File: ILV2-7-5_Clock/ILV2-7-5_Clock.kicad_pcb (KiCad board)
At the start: 2 copper layers, 61 parts, among them J1 CONN_01X05, J2 USB_OTG, Q1 BSS84, Q2 BSS138, Q3 BSS84, Q4 BSS138, SW1 TACT_SWITCH, SW2 TACT_SWITCH, SW3 CJS1200, SW4 TACT_SWITCH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

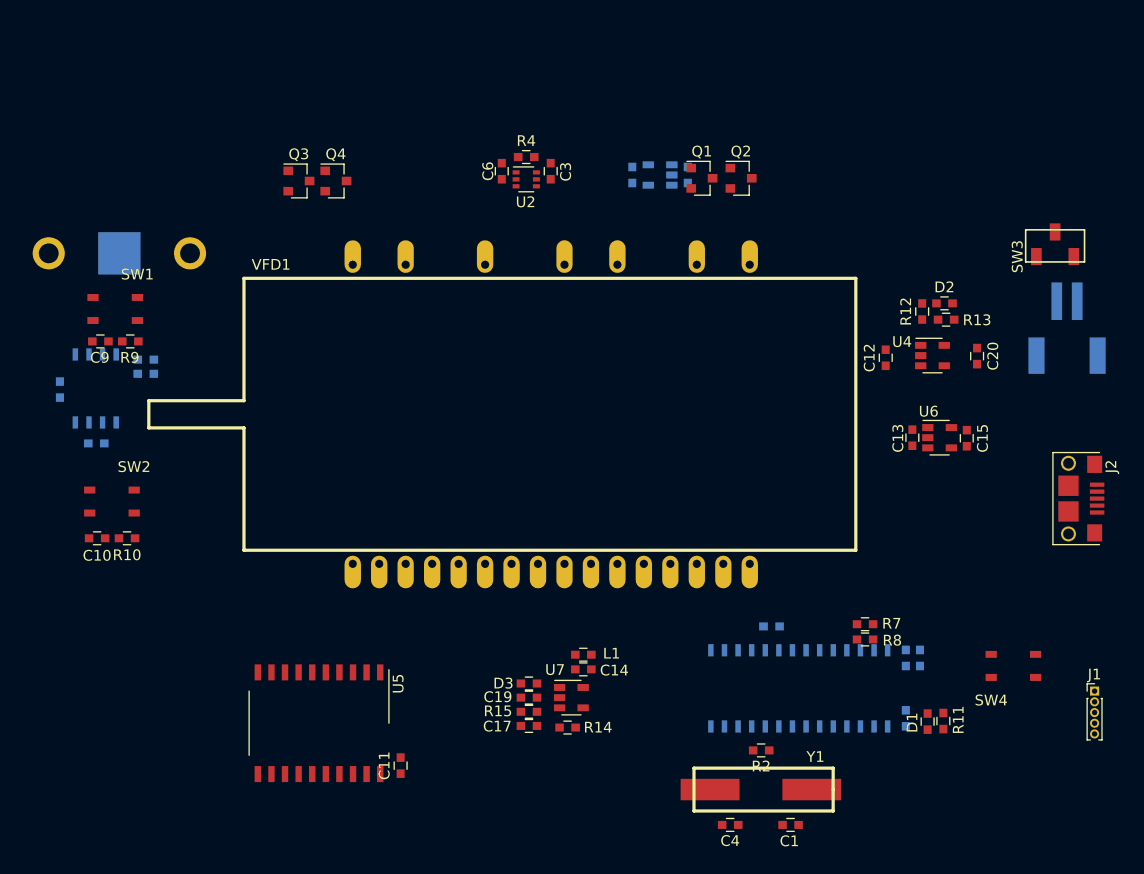
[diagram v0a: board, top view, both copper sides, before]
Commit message: More progress on the PCB and casing down schem issues
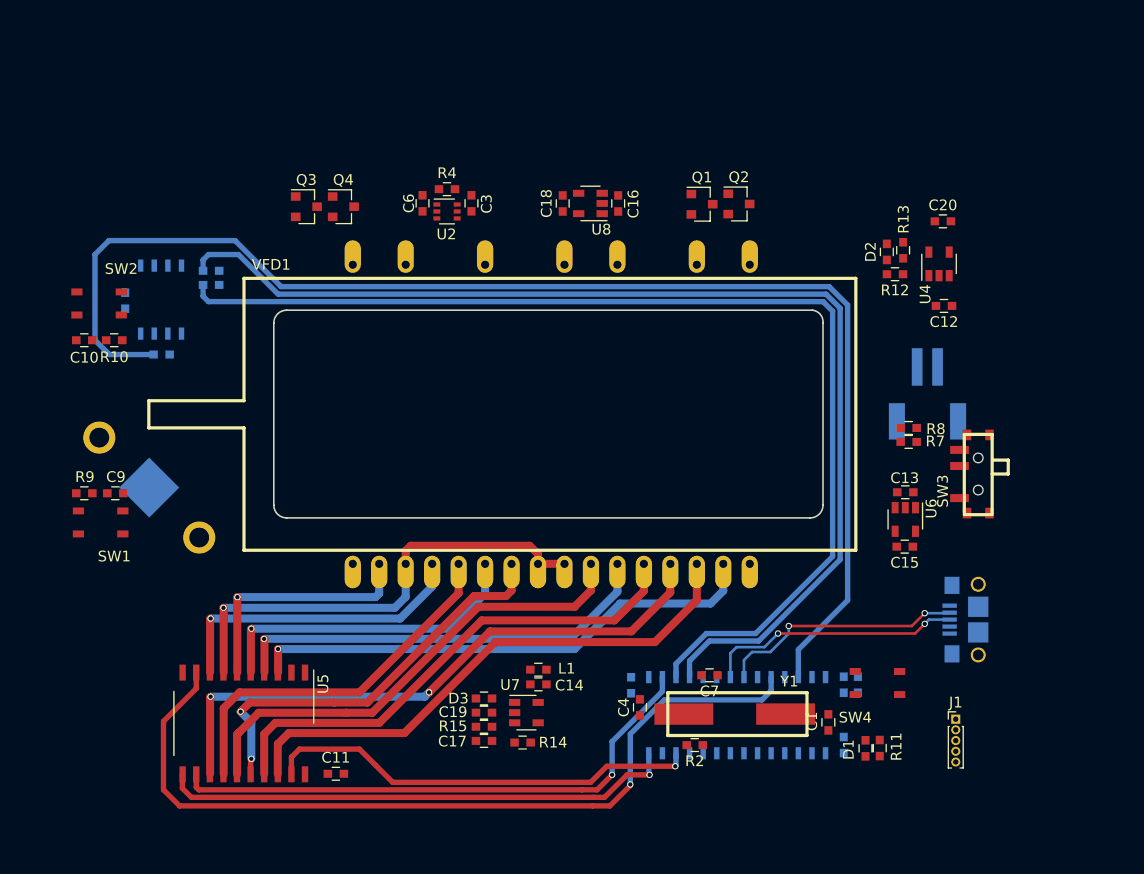
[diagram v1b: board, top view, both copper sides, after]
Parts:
- added C21: 1uF, Capacitors_SMD:C_0603, B.Cu at (151.4, 87.1)
- C16, C18, C7, U8: moved to F.Cu
- J2: moved to B.Cu
- SW3: value CJS1200 -> PCM12SMTR; footprint OpenBCI:CJS-1200TA -> Solutions:PCM12SMTR
- moved SW3 21.0 mm to (183.8, 67.4)
- moved SW1 20.7 mm to (102.7, 72.3), turned to 180 degrees
- moved R8 20.2 mm to (177.3, 63.1)
- moved C10 18.5 mm to (100.3, 54.9)
- moved R10 18.5 mm to (103.1, 54.9)
- moved SW2 18.5 mm to (100.8, 51.1)
- moved BT1 17.8 mm to (101.7, 64.0), turned to 315 degrees
- moved R7 17.5 mm to (177.3, 64.4)
- moved R9 14.8 mm to (100.3, 69.2), turned to 180 degrees
- moved B1 14.4 mm to (180.0, 57.4)
- moved C9 14.3 mm to (103.2, 69.2), turned to 180 degrees
- moved J2 14.1 mm to (183.8, 81.0)
- moved C4 13.8 mm to (152.2, 89.2), turned to 90 degrees
- moved J1 13.2 mm to (181.7, 90.3)
- moved C20 13.0 mm to (180.5, 43.8), turned to 0 degrees
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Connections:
- net /BATT_LEVEL renamed Net-(U3-Pad6)
- C16 pad 1: Net-(C16-Pad1) -> /V_BAT
- U3 pad 26: Net-(U3-Pad26) -> /INT/SQW
- U8 pad 1: Net-(C16-Pad1) -> /V_BAT
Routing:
- net /INT/SQW: track 0.00 -> 124.0 mm
- net /SDA: track 0.00 -> 105.8 mm
- net /SCL: track 0.00 -> 103.4 mm
- net /BLANK: track 0.00 -> 78.1 mm, vias 0 -> 1
- net /f: track 0.00 -> 56.9 mm, vias 0 -> 2
- net /LOAD: track 0.00 -> 51.8 mm, vias 0 -> 1
- net /a: track 0.00 -> 50.9 mm
- net /GRID_5: track 0.00 -> 48.5 mm, vias 0 -> 1
- net /CLK: track 0.00 -> 48.2 mm, vias 0 -> 1
- net /b: track 0.00 -> 47.3 mm
- net /d: track 0.00 -> 44.9 mm
- net /DOT: track 0.00 -> 44.0 mm, vias 0 -> 1
- net /DIN: track 0.00 -> 40.9 mm, vias 0 -> 1
- net /GRID_4: track 0.00 -> 40.6 mm, vias 0 -> 1
- net /c: track 0.00 -> 38.8 mm, vias 0 -> 2
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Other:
- board outline added: 51.3 x 19.4 mm

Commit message: Finished first draft of pub and zone fills
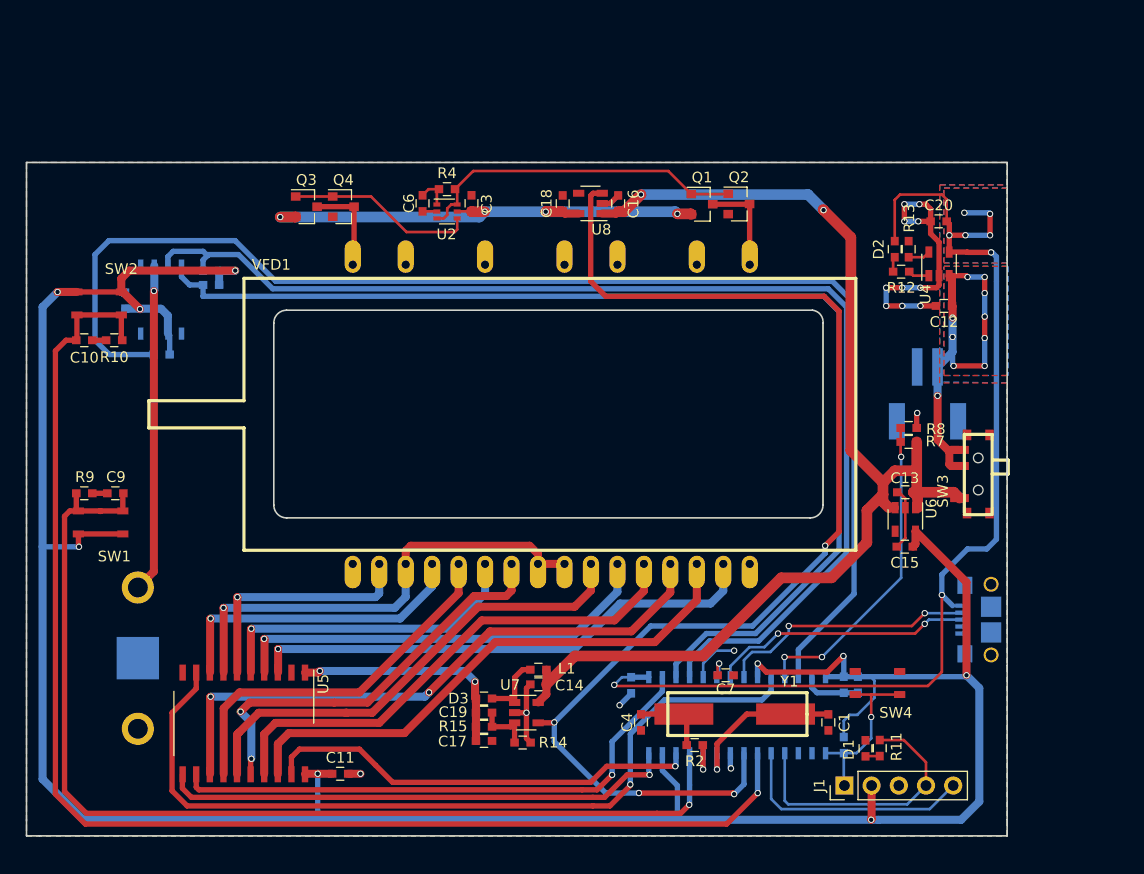
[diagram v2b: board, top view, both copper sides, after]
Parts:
- J1: footprint Pin_Headers:Pin_Header_Straight_1x05_Pitch1.00mm -> Pin_Headers:Pin_Header_Straight_1x05_Pitch2.54mm
- moved BT1 14.5 mm to (105.3, 78.0), turned to 270 degrees
- moved J1 12.1 mm to (171.3, 96.5), turned to 90 degrees
- moved C7 1.50 mm to (160.2, 86.2), turned to 0 degrees
- moved C4 1.40 mm to (152.3, 90.6), turned to 270 degrees
- moved J2 1.20 mm to (185.0, 81.0)
- moved D2 0.78 mm to (176.0, 46.4)
- moved R12 0.62 mm to (176.6, 48.5)
- moved R13 0.53 mm to (177.3, 46.4)
- moved C11 0.40 mm to (124.2, 95.4)
- moved C20 0.40 mm to (180.1, 43.8)
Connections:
- net Net-(B1-Pad1) renamed /BAT_CHRG
- C13 pad 2: Net-(C13-Pad2) -> GND
- C15 pad 2: Net-(C13-Pad2) -> GND
- C20 pad 2: /V_BUS -> +5V
- D2 pad 2: /V_BUS -> +5V
- J2 pad 1: /V_BUS -> +5V
- J2 pad 10: (no net) -> GND
- J2 pad 11: (no net) -> GND
- J2 pad 7: (no net) -> GND
- J2 pad 8: (no net) -> GND
- J2 pad 9: (no net) -> GND
- SW3 pad 4: (no net) -> GND
- SW3 pad 5: (no net) -> GND
- SW3 pad 6: (no net) -> GND
- SW3 pad 7: (no net) -> GND
- U3 pad 2: /SWITCH_1 -> Net-(U3-Pad2)
- U3 pad 6: Net-(U3-Pad6) -> /SWITCH_1
- U4 pad 4: /V_BUS -> +5V
- U6 pad 2: Net-(C13-Pad2) -> GND
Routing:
- net +3V3: track 0.00 -> 256.5 mm, vias 0 -> 9
- net /SWITCH_1: track 0.00 -> 124.4 mm, vias 0 -> 1
- net /VFD_EN: track 0.00 -> 114.9 mm, vias 0 -> 4
- net /V_BAT: track 0.00 -> 111.5 mm, vias 0 -> 2
- net +5V: track 0.00 -> 106.2 mm, vias 0 -> 8
- net /BOOT_EN: track 0.00 -> 99.2 mm, vias 0 -> 1
- net GND: track 0.00 -> 59.7 mm, vias 0 -> 16
- net +2V5: track 0.00 -> 45.9 mm, vias 0 -> 4
- net /BAT_CHRG: track 0.00 -> 38.1 mm, vias 0 -> 10
- net /H_BridgeA: track 0.00 -> 31.4 mm
- net Net-(BT1-Pad1): track 0.00 -> 30.7 mm, vias 0 -> 1
- net /BAT_SENS: track 0.00 -> 29.9 mm, vias 0 -> 3
- net /PGD: track 0.00 -> 26.1 mm
- net /PGC: track 0.00 -> 22.6 mm
- net +24V: track 0.00 -> 21.9 mm, vias 0 -> 2
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- added copper zone on B.Cu, net +5V
- added copper zone on F.Cu, net +5V
- added copper zone on B.Cu, net /BAT_CHRG
- added copper zone on F.Cu, net /BAT_CHRG
- added copper zone on B.Cu, net GND
- added copper zone on F.Cu, net GND
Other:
- board size 51.3 x 19.4 mm -> 91.6 x 62.9 mm

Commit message: Added mount holes, fixed the inductor footprint size
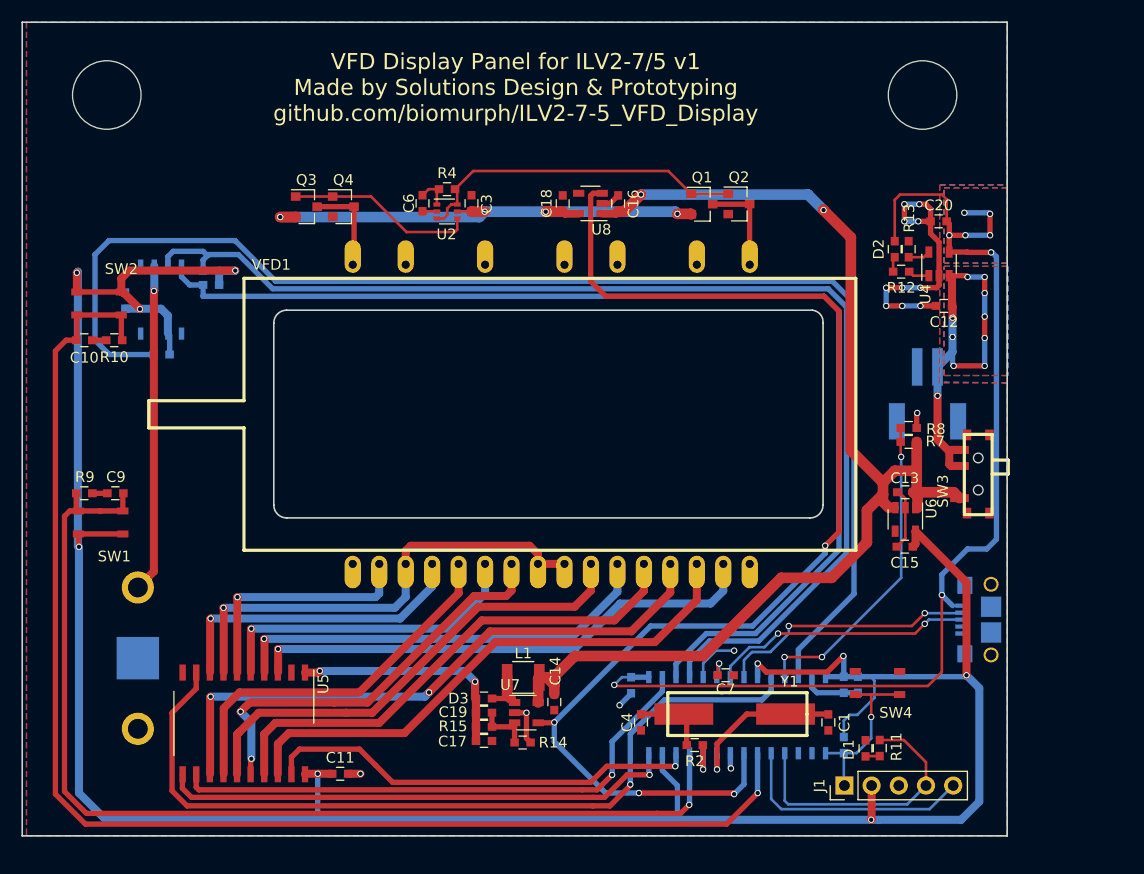
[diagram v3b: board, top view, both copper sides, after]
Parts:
- added REF**: MountingHole_6.4mm_M6, Mounting_Holes:MountingHole_6.4mm_M6, F.Cu at (178.6, 32.0)
- added REF**: MountingHole_6.4mm_M6, Mounting_Holes:MountingHole_6.4mm_M6, F.Cu at (102.4, 32.0)
- L1: footprint Capacitors_SMD:C_0603 -> Capacitors_SMD:C_1210
- moved C14 2.22 mm to (144.2, 88.7), turned to 270 degrees
- moved L1 1.59 mm to (141.3, 86.4)
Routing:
- net +3V3: track 256.5 -> 251.7 mm
- net GND: track 59.7 -> 56.9 mm
- net Net-(D3-Pad2): track 6.37 -> 4.37 mm
- net /V_BAT: track 111.5 -> 112.7 mm
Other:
- board size 91.6 x 62.9 mm -> 92 x 76 mm
- board text added: "VFD Display Panel for ILV2-7/5 v1 Made by Solutions Design & Prototyping github.com/biomurph/ILV2-7-5_VFD_Display"
